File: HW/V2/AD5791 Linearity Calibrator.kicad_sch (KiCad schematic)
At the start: 49 parts, among them J11 PWR, J11 SIG, J2 VREFP, J3 VREFN, J5 VREFP, SW1 RST, U11 L79L15, U12 7533, U13 ADuM1400xRW, U2 AD5791BRUZ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

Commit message: updated files
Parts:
- removed H1, H2: MountingHole_Pad, MountingHole:MountingHole_3.2mm_M3_DIN965_Pad, symbol Mechanical:MountingHole_Pad
- added J8: VREFN, Connector_PinHeader_1.27mm:PinHeader_1x02_P1.27mm_Vertical, symbol Connector_Generic:Conn_01x02
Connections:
- net GND: now also J8.1 (Pin_1), J8.2 (Pin_2)
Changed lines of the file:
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@@
   (junction (at 185.42 237.49) (diameter 0) (color 0 0 0 0)
   )
-  (junction (at 240.03 261.62) (diameter 0) (color 0 0 0 0)
-  )
   (junction (at 76.2 226.06) (diameter 0) (color 0 0 0 0)
   )
@@
   (junction (at 175.26 237.49) (diameter 0) (color 0 0 0 0)
   )
+  (junction (at 223.52 215.9) (diameter 0) (color 0 0 0 0)
+  )
   (junction (at 62.23 113.03) (diameter 0) (color 0 0 0 0)
   )
@@
     (stroke (width 0) (type default))
   )
-  (wire (pts (xy 240.03 261.62) (xy 240.03 255.27))
-    (stroke (width 0) (type default))
-  )
   (wire (pts (xy 46.99 246.38) (xy 46.99 243.84))
     (stroke (width 0) (type default))
@@
     (stroke (width 0) (type default))
   )
-  (wire (pts (xy 240.03 255.27) (xy 242.57 255.27))
-    (stroke (width 0) (type default))
-  )
   (wire (pts (xy 76.2 248.92) (xy 76.2 246.38))
     (stroke (width 0) (type default))
@@
     (stroke (width 0) (type default))
   )
+  (wire (pts (xy 220.98 213.36) (xy 223.52 213.36))
+    (stroke (width 0) (type default))
+  )
   (wire (pts (xy 34.29 118.11) (xy 34.29 115.57))
     (stroke (width 0) (type default))
@@
     (stroke (width 0) (type default))
   )
+  (wire (pts (xy 223.52 215.9) (xy 220.98 215.9))
+    (stroke (width 0) (type default))
+  )
   (wire (pts (xy 105.41 226.06) (xy 105.41 228.6))
     (stroke (width 0) (type default))
@@
     (stroke (width 0) (type default))
   )
-  (wire (pts (xy 240.03 261.62) (xy 242.57 261.62))
-    (stroke (width 0) (type default))
-  )
   (wire (pts (xy 175.26 237.49) (xy 185.42 237.49))
     (stroke (width 0) (type default))
@@
     (stroke (width 0) (type default))
   )
+  (wire (pts (xy 223.52 215.9) (xy 223.52 218.44))
+    (stroke (width 0) (type default))
+  )
   (wire (pts (xy 158.75 137.16) (xy 168.91 137.16))
     (stroke (width 0) (type default))
@@
     (stroke (width 0) (type default))
   )
+  (wire (pts (xy 223.52 213.36) (xy 223.52 215.9))
+    (stroke (width 0) (type default))
+  )
   (wire (pts (xy 302.26 105.41) (xy 302.26 102.87))
     (stroke (width 0) (type default))
@@
     (stroke (width 0) (type default))
   )
-  (wire (pts (xy 240.03 264.16) (xy 240.03 261.62))
-    (stroke (width 0) (type default))
-  )
   (wire (pts (xy 313.69 77.47) (xy 314.96 77.47))
     (stroke (width 0) (type default))
@@
     )
   )
-  (symbol (lib_id "power:GND") (at 240.03 264.16 0) (unit 1)
-    (in_bom yes) (on_board yes) (dnp no) (fields_autoplaced)
-    (property "Reference" "#PWR016" (at 240.03 270.51 0)
-      (effects (font (size 1.27 1.27)) hide)
-    )
-    (property "Value" "GND" (at 240.03 269.24 0)
-      (effects (font (size 1.27 1.27)))
-    )
-    (property "Footprint" "" (at 240.03 264.16 0)
-      (effects (font (size 1.27 1.27)) hide)
-    )
-    (property "Datasheet" "" (at 240.03 264.16 0)
-      (effects (font (size 1.27 1.27)) hide)
-    )
-    (pin "1")
-    (instances
-      (project "AD5791 Linearity Calibrator"
-        (path "/e4c8fe5c-4d6c-45a9-911b-05eafd37681e"
-          (reference "#PWR016") (unit 1)
-        )
-      )
-    )
-  )
   (symbol (lib_id "Device:R_Pack08_Split") (at 62.23 96.52 0) (unit 6)
     (in_bom yes) (on_board yes) (dnp no)
@@
     )
   )
-  (symbol (lib_id "Mechanical:MountingHole_Pad") (at 245.11 255.27 270) (unit 1)
-    (in_bom yes) (on_board yes) (dnp no) (fields_autoplaced)
-    (property "Reference" "H1" (at 248.92 254 90)
-      (effects (font (size 1.27 1.27)) (justify left))
-    )
-    (property "Value" "MountingHole_Pad" (at 248.92 256.54 90)
-      (effects (font (size 1.27 1.27)) (justify left))
-    )
-    (property "Footprint" "MountingHole:MountingHole_3.2mm_M3_DIN965_Pad" (at 245.11 255.27 0)
-      (effects (font (size 1.27 1.27)) hide)
-    )
-    (property "Datasheet" "~" (at 245.11 255.27 0)
-      (effects (font (size 1.27 1.27)) hide)
-    )
-    (pin "1")
-    (instances
-      (project "AD5791 Linearity Calibrator"
-        (path "/e4c8fe5c-4d6c-45a9-911b-05eafd37681e"
-          (reference "H1") (unit 1)
-        )
-      )
-    )
-  )
   (symbol (lib_id "power:+15V") (at 76.2 213.36 0) (unit 1)
     (in_bom yes) (on_board yes) (dnp no) (fields_autoplaced)
@@
     )
   )
+  (symbol (lib_id "power:GND") (at 223.52 218.44 0) (unit 1)
+    (in_bom yes) (on_board yes) (dnp no) (fields_autoplaced)
+    (property "Reference" "#PWR027" (at 223.52 224.79 0)
+      (effects (font (size 1.27 1.27)) hide)
+    )
+    (property "Value" "GND" (at 223.52 223.52 0)
+      (effects (font (size 1.27 1.27)))
+    )
+    (property "Footprint" "" (at 223.52 218.44 0)
+      (effects (font (size 1.27 1.27)) hide)
+    )
+    (property "Datasheet" "" (at 223.52 218.44 0)
+      (effects (font (size 1.27 1.27)) hide)
+    )
+    (pin "1")
+    (instances
+      (project "AD5791 Linearity Calibrator"
+        (path "/545249ea-2c8e-4b30-8f2b-5f4518163292"
+          (reference "#PWR027") (unit 1)
+        )
+      )
+      (project "AD5791 Linearity Calibrator"
+        (path "/e4c8fe5c-4d6c-45a9-911b-05eafd37681e"
+          (reference "#PWR048") (unit 1)
+        )
+      )
+    )
+  )
   (symbol (lib_id "power:+15V") (at 278.13 238.76 270) (unit 1)
     (in_bom yes) (on_board yes) (dnp no) (fields_autoplaced)
@@
     )
   )
-  (symbol (lib_id "Mechanical:MountingHole_Pad") (at 245.11 261.62 270) (unit 1)
+  (symbol (lib_id "Connector_Generic:Conn_01x02") (at 215.9 213.36 0) (mirror y) (unit 1)
     (in_bom yes) (on_board yes) (dnp no) (fields_autoplaced)
-    (property "Reference" "H2" (at 248.92 260.35 90)
-      (effects (font (size 1.27 1.27)) (justify left))
+    (property "Reference" "J8" (at 215.9 207.01 0)
+      (effects (font (size 1.27 1.27)))
     )
-    (property "Value" "MountingHole_Pad" (at 248.92 262.89 90)
-      (effects (font (size 1.27 1.27)) (justify left))
+    (property "Value" "VREFN" (at 215.9 209.55 0)
+      (effects (font (size 1.27 1.27)))
     )
-    (property "Footprint" "MountingHole:MountingHole_3.2mm_M3_DIN965_Pad" (at 245.11 261.62 0)
+    (property "Footprint" "Connector_PinHeader_1.27mm:PinHeader_1x02_P1.27mm_Vertical" (at 215.9 213.36 0)
       (effects (font (size 1.27 1.27)) hide)
     )
-    (property "Datasheet" "~" (at 245.11 261.62 0)
+    (property "Datasheet" "~" (at 215.9 213.36 0)
       (effects (font (size 1.27 1.27)) hide)
     )
     (pin "1")
+    (pin "2")
     (instances
       (project "AD5791 Linearity Calibrator"
         (path "/e4c8fe5c-4d6c-45a9-911b-05eafd37681e"
-          (reference "H2") (unit 1)
+          (reference "J8") (unit 1)
         )
       )

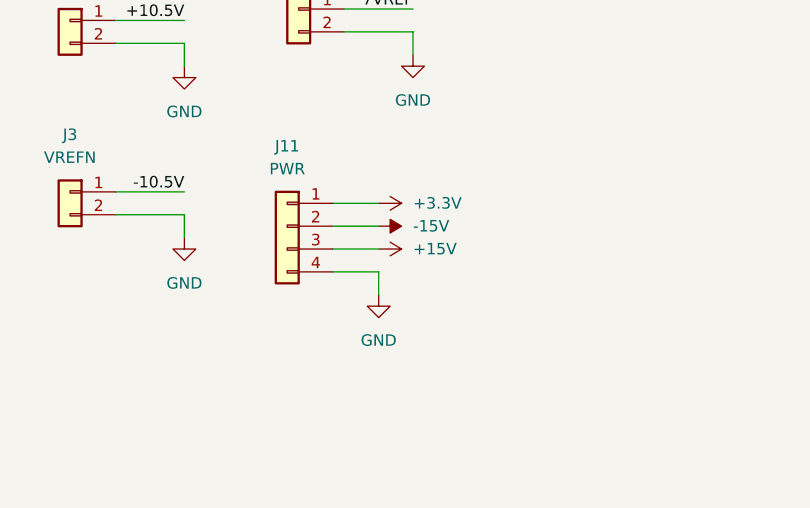
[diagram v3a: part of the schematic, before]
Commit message: updated layout
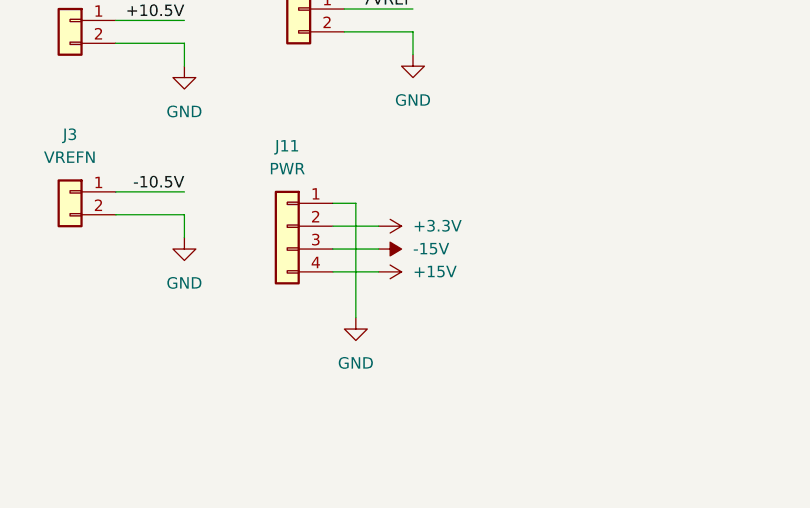
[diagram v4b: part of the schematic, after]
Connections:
- net +15V: now also J11.4 (Pin_4); no longer J11.3 (Pin_3)
- net +3.3V: now also J11.2 (Pin_2); no longer J11.1 (Pin_1)
- net -15V: now also J11.3 (Pin_3); no longer J11.2 (Pin_2)
- net GND: now also J11.1 (Pin_1); no longer J11.4 (Pin_4)
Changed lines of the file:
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@@
     (stroke (width 0) (type default))
   )
-  (wire (pts (xy 278.13 241.3) (xy 278.13 243.84))
+  (wire (pts (xy 275.59 233.68) (xy 275.59 246.38))
     (stroke (width 0) (type default))
   )
@@
     (stroke (width 0) (type default))
   )
-  (wire (pts (xy 273.05 238.76) (xy 278.13 238.76))
+  (wire (pts (xy 273.05 241.3) (xy 278.13 241.3))
     (stroke (width 0) (type default))
   )
@@
     (stroke (width 0) (type default))
   )
+  (wire (pts (xy 275.59 233.68) (xy 273.05 233.68))
+    (stroke (width 0) (type default))
+  )
   (wire (pts (xy 240.03 97.79) (xy 240.03 116.84))
     (stroke (width 0) (type default))
@@
     (stroke (width 0) (type default))
   )
-  (wire (pts (xy 278.13 241.3) (xy 273.05 241.3))
-    (stroke (width 0) (type default))
-  )
   (wire (pts (xy 111.76 64.77) (xy 138.43 64.77))
     (stroke (width 0) (type default))
@@
     (stroke (width 0) (type default))
   )
-  (wire (pts (xy 273.05 236.22) (xy 278.13 236.22))
+  (wire (pts (xy 273.05 238.76) (xy 278.13 238.76))
     (stroke (width 0) (type default))
   )
@@
     (stroke (width 0) (type default))
   )
-  (wire (pts (xy 273.05 233.68) (xy 278.13 233.68))
+  (wire (pts (xy 273.05 236.22) (xy 278.13 236.22))
     (stroke (width 0) (type default))
   )
@@
     )
   )
-  (symbol (lib_id "power:+3.3V") (at 278.13 233.68 270) (unit 1)
+  (symbol (lib_id "power:+3.3V") (at 278.13 236.22 270) (unit 1)
     (in_bom yes) (on_board yes) (dnp no) (fields_autoplaced)
-    (property "Reference" "#PWR041" (at 274.32 233.68 0)
+    (property "Reference" "#PWR041" (at 274.32 236.22 0)
       (effects (font (size 1.27 1.27)) hide)
     )
-    (property "Value" "+3.3V" (at 281.94 233.68 90)
+    (property "Value" "+3.3V" (at 281.94 236.22 90)
       (effects (font (size 1.27 1.27)) (justify left))
     )
-    (property "Footprint" "" (at 278.13 233.68 0)
+    (property "Footprint" "" (at 278.13 236.22 0)
       (effects (font (size 1.27 1.27)) hide)
     )
-    (property "Datasheet" "" (at 278.13 233.68 0)
+    (property "Datasheet" "" (at 278.13 236.22 0)
       (effects (font (size 1.27 1.27)) hide)
     )
@@
     )
   )
-  (symbol (lib_id "power:+15V") (at 278.13 238.76 270) (unit 1)
+  (symbol (lib_id "power:+15V") (at 278.13 241.3 270) (unit 1)
     (in_bom yes) (on_board yes) (dnp no) (fields_autoplaced)
-    (property "Reference" "#PWR034" (at 274.32 238.76 0)
+    (property "Reference" "#PWR034" (at 274.32 241.3 0)
       (effects (font (size 1.27 1.27)) hide)
     )
-    (property "Value" "+15V" (at 281.94 238.76 90)
+    (property "Value" "+15V" (at 281.94 241.3 90)
       (effects (font (size 1.27 1.27)) (justify left))
     )
-    (property "Footprint" "" (at 278.13 238.76 0)
+    (property "Footprint" "" (at 278.13 241.3 0)
       (effects (font (size 1.27 1.27)) hide)
     )
-    (property "Datasheet" "" (at 278.13 238.76 0)
+    (property "Datasheet" "" (at 278.13 241.3 0)
       (effects (font (size 1.27 1.27)) hide)
     )
@@
     )
   )
-  (symbol (lib_id "power:GND") (at 278.13 243.84 0) (unit 1)
+  (symbol (lib_id "power:GND") (at 275.59 246.38 0) (unit 1)
     (in_bom yes) (on_board yes) (dnp no)
-    (property "Reference" "#PWR027" (at 278.13 250.19 0)
+    (property "Reference" "#PWR027" (at 275.59 252.73 0)
       (effects (font (size 1.27 1.27)) hide)
     )
-    (property "Value" "GND" (at 278.13 248.92 0)
+    (property "Value" "GND" (at 275.59 251.46 0)
       (effects (font (size 1.27 1.27)))
     )
-    (property "Footprint" "" (at 278.13 243.84 0)
+    (property "Footprint" "" (at 275.59 246.38 0)
       (effects (font (size 1.27 1.27)) hide)
     )
-    (property "Datasheet" "" (at 278.13 243.84 0)
+    (property "Datasheet" "" (at 275.59 246.38 0)
       (effects (font (size 1.27 1.27)) hide)
     )
@@
     )
   )
-  (symbol (lib_id "power:-15V") (at 278.13 236.22 270) (unit 1)
+  (symbol (lib_id "power:-15V") (at 278.13 238.76 270) (unit 1)
     (in_bom yes) (on_board yes) (dnp no) (fields_autoplaced)
-    (property "Reference" "#PWR033" (at 280.67 236.22 0)
+    (property "Reference" "#PWR033" (at 280.67 238.76 0)
       (effects (font (size 1.27 1.27)) hide)
     )
-    (property "Value" "-15V" (at 281.94 236.22 90)
+    (property "Value" "-15V" (at 281.94 238.76 90)
       (effects (font (size 1.27 1.27)) (justify left))
     )
-    (property "Footprint" "" (at 278.13 236.22 0)
+    (property "Footprint" "" (at 278.13 238.76 0)
       (effects (font (size 1.27 1.27)) hide)
     )
-    (property "Datasheet" "" (at 278.13 236.22 0)
+    (property "Datasheet" "" (at 278.13 238.76 0)
       (effects (font (size 1.27 1.27)) hide)
     )
